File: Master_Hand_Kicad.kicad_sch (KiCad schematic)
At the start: 0 parts

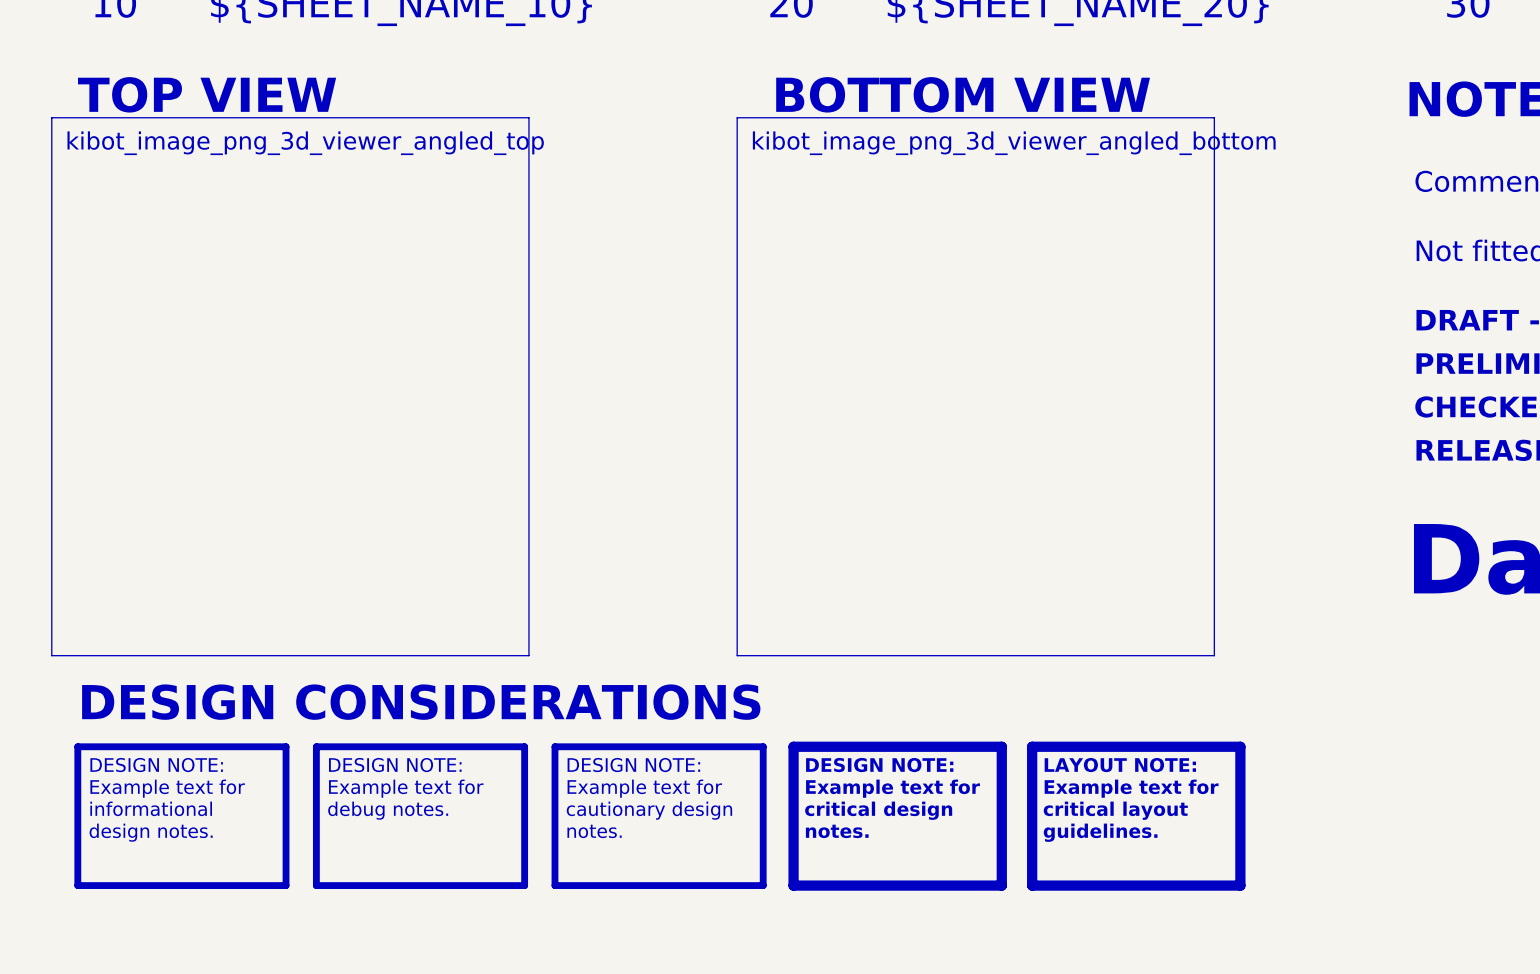
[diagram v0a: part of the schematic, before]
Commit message: [23/06/2026] Block Diagram update
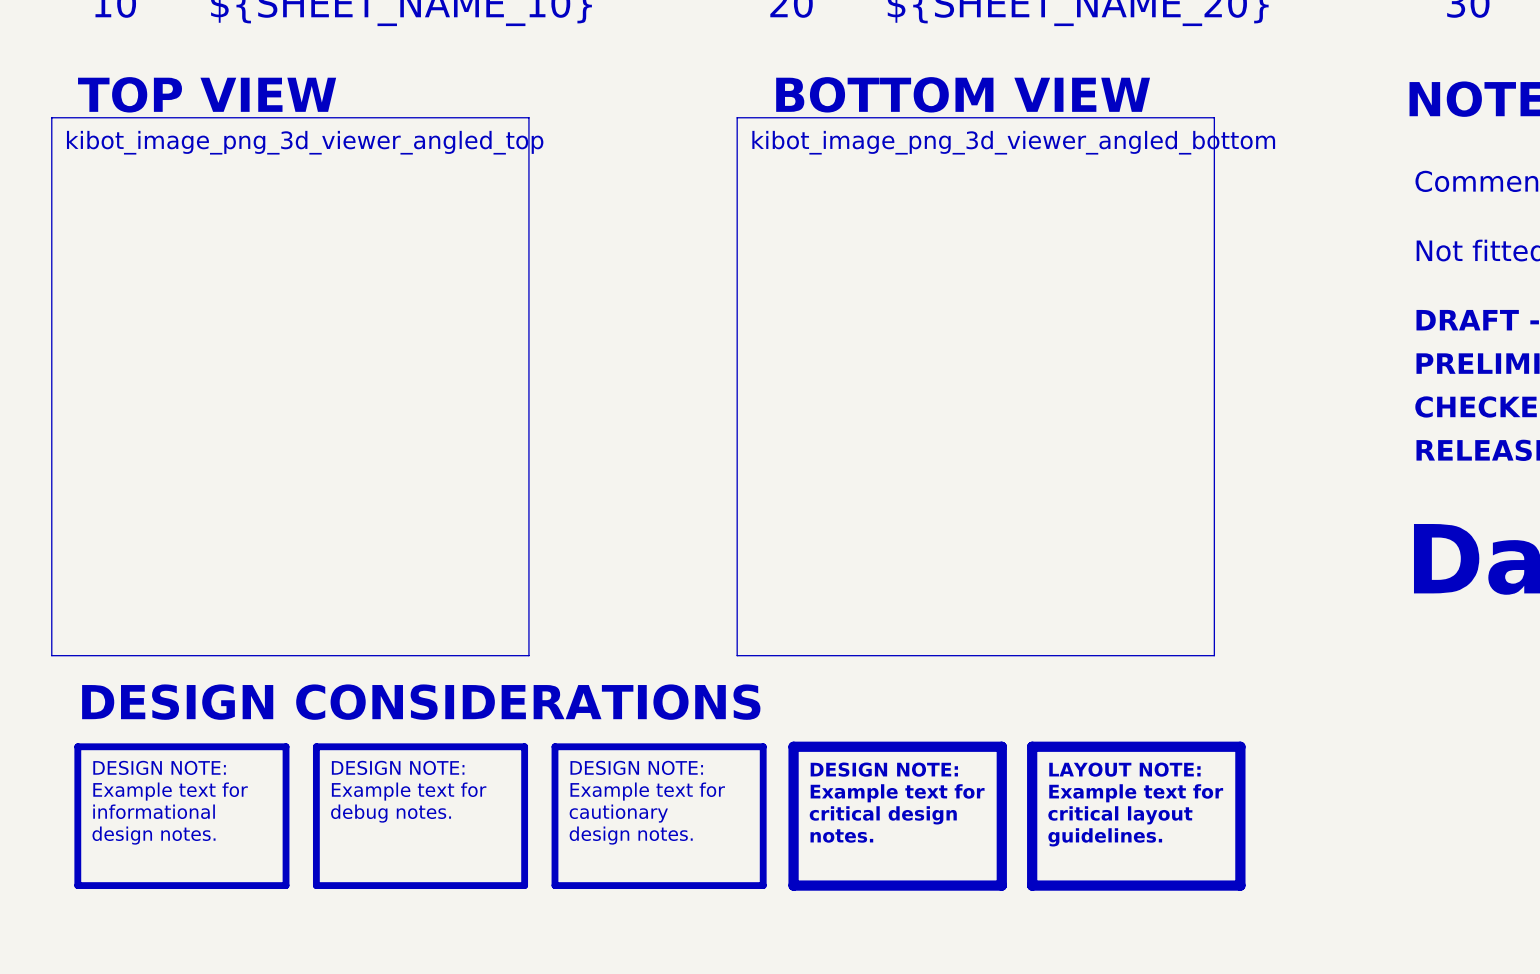
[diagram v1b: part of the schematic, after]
